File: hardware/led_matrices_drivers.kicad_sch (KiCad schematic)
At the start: 12 parts, among them U6 MAX7219, U7 MAX7219, U8 MAX7219, U9 MAX7219

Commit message: Removed comments on UART, added some footprints and started fixing rule checks
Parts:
- C12, C13, C14, C15: Manuf. Part # (none) -> GRM21BR71H104KA01L; Part Num GRM21BR71H104KA01L -> (none); Price/unit $0.0097 -> (none); Supplier Name (none) -> JLCPCB; Supplier Unit Price (none) -> $0.0097
- R10, R11, R12, R9: Manuf. Part # (none) -> CR0805F89531G; Part Num CR0805F89531G -> (none); Price/unit $0.0022 -> (none); Supplier Unit Price (none) -> $0.0022
- U6, U7, U8, U9: Manuf. Part # (none) -> MAX7219CWG+T; Part Num MAX7219CWG+T -> (none); Price/unit $2.6325 -> (none); Supplier Name (none) -> JLCPCB; Supplier Unit Price (none) -> $2.6325
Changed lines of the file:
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@@
 			)
 		)
-		(property "Part Num" "MAX7219CWG+T"
+		(property "Supplier Link" "https://jlcpcb.com/partdetail/10499-MAX7219CWGT/C9964"
 			(at 107.95 93.98 0)
 			(effects
@@
 			)
 		)
-		(property "Price/unit" "$2.6325"
+		(property "Supplier Name" "JLCPCB"
 			(at 107.95 93.98 0)
 			(effects
@@
 			)
 		)
-		(property "Supplier Link" "https://jlcpcb.com/partdetail/10499-MAX7219CWGT/C9964"
+		(property "Manuf. Part #" "MAX7219CWG+T"
+			(at 107.95 93.98 0)
+			(effects
+				(font
+					(size 1.27 1.27)
+				)
+				(hide yes)
+			)
+		)
+		(property "Supplier Unit Price" "$2.6325"
 			(at 107.95 93.98 0)
 			(effects
@@
 			)
 		)
-		(property "Part Num" "CR0805F89531G"
+		(property "Supplier Link" ""
 			(at 154.94 67.31 0)
 			(effects
@@
 			)
 		)
-		(property "Price/unit" " $0.0022"
+		(property "Supplier Name" ""
 			(at 154.94 67.31 0)
 			(effects
@@
 			)
 		)
-		(property "Supplier Link" ""
+		(property "Manuf. Part #" "CR0805F89531G"
+			(at 154.94 67.31 0)
+			(effects
+				(font
+					(size 1.27 1.27)
+				)
+				(hide yes)
+			)
+		)
+		(property "Supplier Unit Price" " $0.0022"
 			(at 154.94 67.31 0)
 			(effects
@@
 			)
 		)
-		(property "Part Num" "CR0805F89531G"
+		(property "Supplier Link" ""
 			(at 95.25 67.31 0)
 			(effects
@@
 			)
 		)
-		(property "Price/unit" " $0.0022"
+		(property "Supplier Name" ""
 			(at 95.25 67.31 0)
 			(effects
@@
 			)
 		)
-		(property "Supplier Link" ""
+		(property "Manuf. Part #" "CR0805F89531G"
+			(at 95.25 67.31 0)
+			(effects
+				(font
+					(size 1.27 1.27)
+				)
+				(hide yes)
+			)
+		)
+		(property "Supplier Unit Price" " $0.0022"
 			(at 95.25 67.31 0)
 			(effects
@@
 			)
 		)
-		(property "Part Num" "MAX7219CWG+T"
+		(property "Supplier Link" "https://jlcpcb.com/partdetail/10499-MAX7219CWGT/C9964"
 			(at 229.87 93.98 0)
 			(effects
@@
 			)
 		)
-		(property "Price/unit" "$2.6325"
+		(property "Supplier Name" "JLCPCB"
 			(at 229.87 93.98 0)
 			(effects
@@
 			)
 		)
-		(property "Supplier Link" "https://jlcpcb.com/partdetail/10499-MAX7219CWGT/C9964"
+		(property "Manuf. Part #" "MAX7219CWG+T"
+			(at 229.87 93.98 0)
+			(effects
+				(font
+					(size 1.27 1.27)
+				)
+				(hide yes)
+			)
+		)
+		(property "Supplier Unit Price" "$2.6325"
 			(at 229.87 93.98 0)
 			(effects
@@
 			)
 		)
-		(property "Price/unit" " $0.0022"
+		(property "Package" "0805"
 			(at 34.29 67.31 0)
 			(effects
@@
 			)
 		)
-		(property "Part Num" "CR0805F89531G"
+		(property "Supplier Name" ""
 			(at 34.29 67.31 0)
 			(effects
@@
 			)
 		)
-		(property "Package" "0805"
+		(property "Manuf. Part #" "CR0805F89531G"
+			(at 34.29 67.31 0)
+			(effects
+				(font
+					(size 1.27 1.27)
+				)
+				(hide yes)
+			)
+		)
+		(property "Supplier Unit Price" " $0.0022"
 			(at 34.29 67.31 0)
 			(effects
@@
 			)
 		)
-		(property "Price/unit" "$2.6325"
+		(property "Package" "SOIC-24-300mil"
 			(at 46.99 93.98 0)
 			(effects
@@
 			)
 		)
-		(property "Part Num" "MAX7219CWG+T"
+		(property "Supplier Name" "JLCPCB"
 			(at 46.99 93.98 0)
 			(effects
@@
 			)
 		)
-		(property "Package" "SOIC-24-300mil"
+		(property "Manuf. Part #" "MAX7219CWG+T"
+			(at 46.99 93.98 0)
+			(effects
+				(font
+					(size 1.27 1.27)
+				)
+				(hide yes)
+			)
+		)
+		(property "Supplier Unit Price" "$2.6325"
 			(at 46.99 93.98 0)
 			(effects
@@
 			)
 		)
-		(property "Part Num" "GRM21BR71H104KA01L"
+		(property "Supplier Link" "https://jlcpcb.com/partdetail/MurataElectronics-GRM21BR71H104KA01L/C77082"
 			(at 232.41 64.77 0)
 			(effects
@@
 			)
 		)
-		(property "Price/unit" "$0.0097"
+		(property "Supplier Name" "JLCPCB"
 			(at 232.41 64.77 0)
 			(effects
@@
 			)
 		)
-		(property "Supplier Link" "https://jlcpcb.com/partdetail/MurataElectronics-GRM21BR71H104KA01L/C77082"
+		(property "Manuf. Part #" "GRM21BR71H104KA01L"
+			(at 232.41 64.77 0)
+			(effects
+				(font
+					(size 1.27 1.27)
+				)
+				(hide yes)
+			)
+		)
+		(property "Supplier Unit Price" "$0.0097"
 			(at 232.41 64.77 0)
 			(effects
@@
 			)
 		)
-		(property "Part Num" "MAX7219CWG+T"
+		(property "Supplier Link" "https://jlcpcb.com/partdetail/10499-MAX7219CWGT/C9964"
 			(at 167.64 93.98 0)
 			(effects
@@
 			)
 		)
-		(property "Price/unit" "$2.6325"
+		(property "Supplier Name" "JLCPCB"
 			(at 167.64 93.98 0)
 			(effects
@@
 			)
 		)
-		(property "Supplier Link" "https://jlcpcb.com/partdetail/10499-MAX7219CWGT/C9964"
+		(property "Manuf. Part #" "MAX7219CWG+T"
+			(at 167.64 93.98 0)
+			(effects
+				(font
+					(size 1.27 1.27)
+				)
+				(hide yes)
+			)
+		)
+		(property "Supplier Unit Price" "$2.6325"
 			(at 167.64 93.98 0)
 			(effects
@@
 			)
 		)
-		(property "Part Num" "GRM21BR71H104KA01L"
+		(property "Supplier Link" "https://jlcpcb.com/partdetail/MurataElectronics-GRM21BR71H104KA01L/C77082"
 			(at 170.18 64.77 0)
 			(effects
@@
 			)
 		)
-		(property "Price/unit" "$0.0097"
+		(property "Supplier Name" "JLCPCB"
 			(at 170.18 64.77 0)
 			(effects
@@
 			)
 		)
-		(property "Supplier Link" "https://jlcpcb.com/partdetail/MurataElectronics-GRM21BR71H104KA01L/C77082"
+		(property "Manuf. Part #" "GRM21BR71H104KA01L"
+			(at 170.18 64.77 0)
+			(effects
+				(font
+					(size 1.27 1.27)
+				)
+				(hide yes)
+			)
+		)
+		(property "Supplier Unit Price" "$0.0097"
 			(at 170.18 64.77 0)
 			(effects
@@
 			)
 		)
-		(property "Part Num" "GRM21BR71H104KA01L"
+		(property "Supplier Link" "https://jlcpcb.com/partdetail/MurataElectronics-GRM21BR71H104KA01L/C77082"
 			(at 110.49 64.77 0)
 			(effects
@@
 			)
 		)
-		(property "Price/unit" "$0.0097"
+		(property "Supplier Name" "JLCPCB"
 			(at 110.49 64.77 0)
 			(effects
@@
 			)
 		)
-		(property "Supplier Link" "https://jlcpcb.com/partdetail/MurataElectronics-GRM21BR71H104KA01L/C77082"
+		(property "Manuf. Part #" "GRM21BR71H104KA01L"
+			(at 110.49 64.77 0)
+			(effects
+				(font
+					(size 1.27 1.27)
+				)
+				(hide yes)
+			)
+		)
+		(property "Supplier Unit Price" "$0.0097"
 			(at 110.49 64.77 0)
 			(effects
@@
 			)
 		)
-		(property "Part Num" "GRM21BR71H104KA01L"
+		(property "Supplier Link" "https://jlcpcb.com/partdetail/MurataElectronics-GRM21BR71H104KA01L/C77082"
 			(at 49.53 64.77 0)
 			(effects
@@
 			)
 		)
-		(property "Price/unit" "$0.0097"
+		(property "Supplier Name" "JLCPCB"
 			(at 49.53 64.77 0)
 			(effects
@@
 			)
 		)
-		(property "Supplier Link" "https://jlcpcb.com/partdetail/MurataElectronics-GRM21BR71H104KA01L/C77082"
+		(property "Manuf. Part #" "GRM21BR71H104KA01L"
+			(at 49.53 64.77 0)
+			(effects
+				(font
+					(size 1.27 1.27)
+				)
+				(hide yes)
+			)
+		)
+		(property "Supplier Unit Price" "$0.0097"
 			(at 49.53 64.77 0)
 			(effects
@@
 			)
 		)
-		(property "Part Num" "CR0805F89531G"
-			(at 217.17 67.31 0)
-			(effects
-				(font
-					(size 1.27 1.27)
-				)
-				(hide yes)
-			)
-		)
-		(property "Price/unit" " $0.0022"
-			(at 217.17 67.31 0)
-			(effects
-				(font
-					(size 1.27 1.27)
-				)
-				(hide yes)
-			)
-		)
 		(property "Supplier Link" ""
 			(at 217.17 67.31 0)
 			(effects
+				(font
+					(size 1.27 1.27)
+				)
+				(hide yes)
+			)
+		)
+		(property "Supplier Name" ""
+			(at 217.17 67.31 0)
+			(effects
+				(font
+					(size 1.27 1.27)
+				)
+				(hide yes)
+			)
+		)
+		(property "Manuf. Part #" "CR0805F89531G"
+			(at 217.17 67.31 0)
+			(effects
+				(font
+					(size 1.27 1.27)
+				)
+				(hide yes)
+			)
+		)
+		(property "Supplier Unit Price" " $0.0022"
+			(at 217.17 67.31 0)
+			(effects

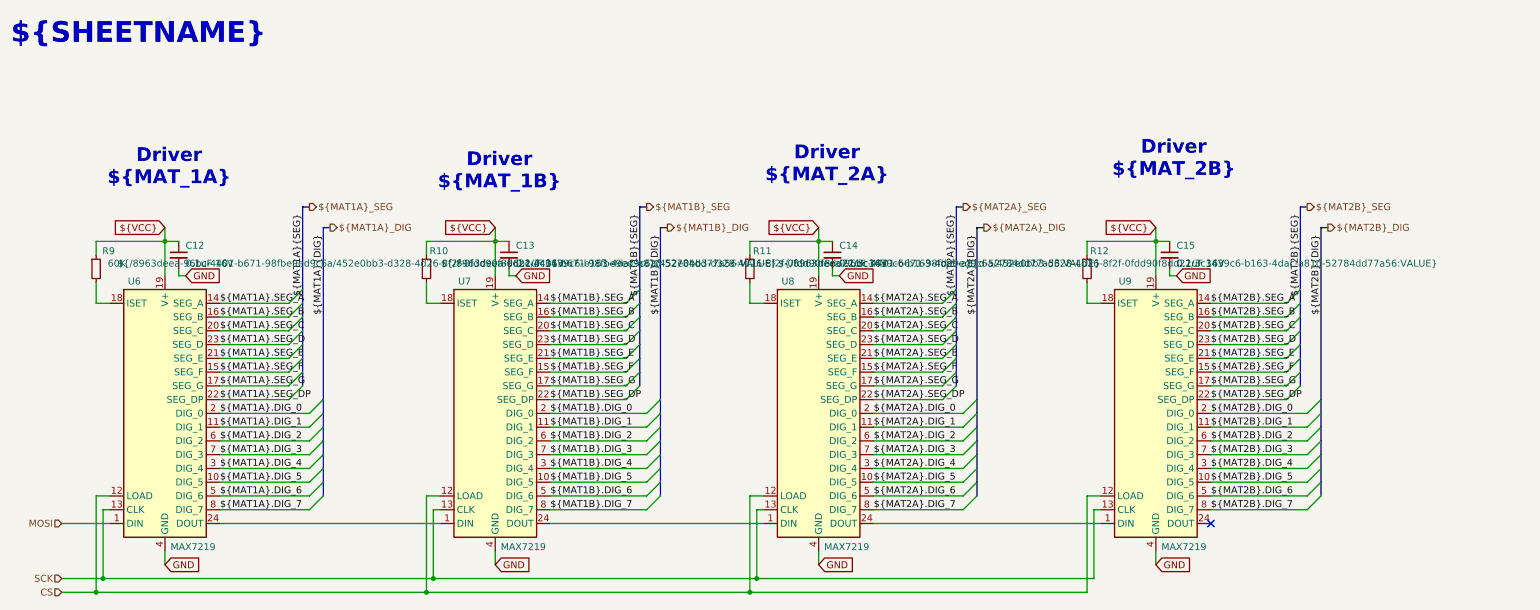
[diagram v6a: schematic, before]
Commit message: Added many footprints and populated part of the property tables
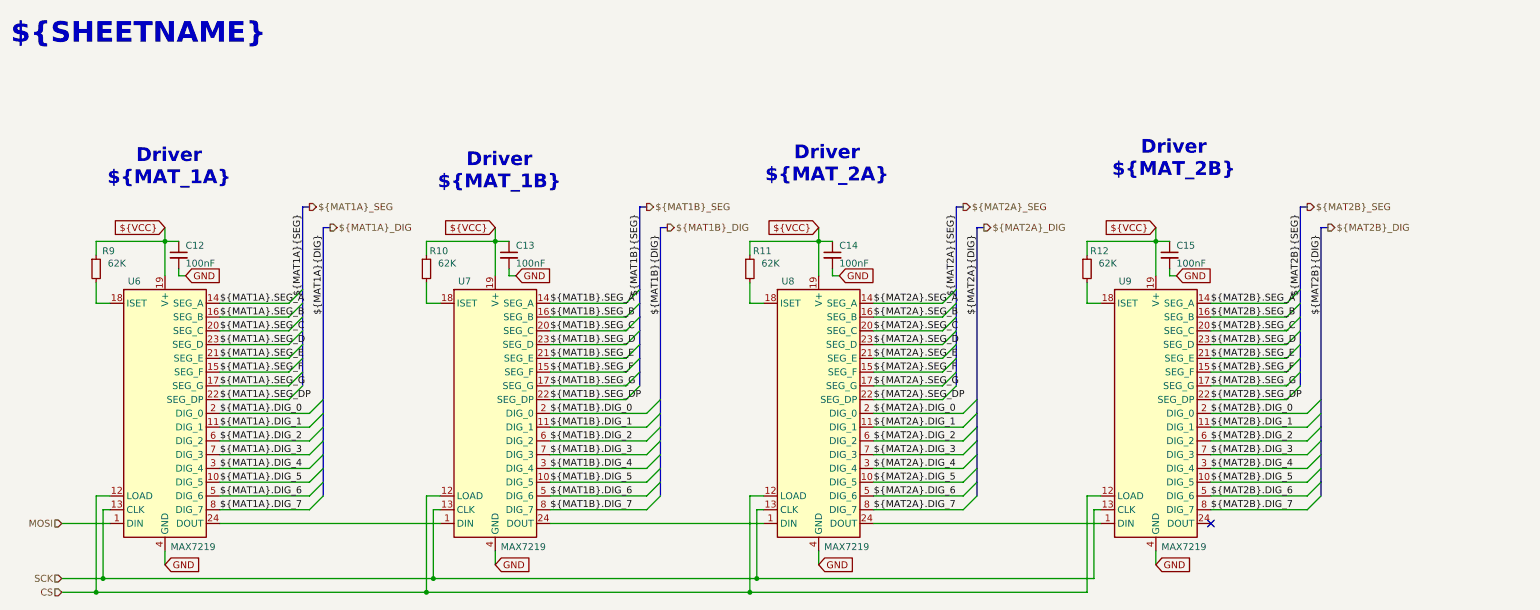
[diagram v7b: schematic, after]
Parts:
- C12, C13, C14, C15: value 0.1uF 16V -> 100nF; footprint (none) -> Capacitor_SMD:C_0805_2012Metric_Pad1.18x1.45mm_HandSolder; Manuf. Name (none) -> Murata Electronics; Supplier Link https://jlcpcb.com/partdetail/MurataElectronics-GRM21BR71H104KA01L/C77082 -> https://jlcpcb.com/partdetail/MurataElectronics-GRM21BR71H104KA01L/C77082; Supplier Part # (none) -> C77082; Supplier Unit Price $0.0097 -> $0.0099
- R10, R11, R12: value ${/8963deea-96bc-4401-b671-98fbe9ed9c6a/452e0bb3-d328-4d26-8f2f-0fdd90f8dd22/3c3439c6-b163-4dac-a81d-52784dd77a56:VALUE} -> 62K; footprint (none) -> Resistor_SMD:R_0805_2012Metric_Pad1.20x1.40mm_HandSolder; Manuf. Name (none) -> UNI-ROYAL(Uniroyal Elec); Manuf. Part # CR0805F89531G -> 0805W8F6202T5E; Supplier Link (none) -> https://jlcpcb.com/partdetail/18471-0805W8F6202T5E/C17783; Supplier Name (none) -> JLCPCB; Supplier Part # (none) -> C17783; Supplier Unit Price $0.0022 -> $0.0019
- R9: value 60K -> 62K; footprint (none) -> Resistor_SMD:R_0805_2012Metric_Pad1.20x1.40mm_HandSolder; Manuf. Name (none) -> UNI-ROYAL(Uniroyal Elec); Manuf. Part # CR0805F89531G -> 0805W8F6202T5E; Supplier Link (none) -> https://jlcpcb.com/partdetail/18471-0805W8F6202T5E/C17783; Supplier Name (none) -> JLCPCB; Supplier Part # (none) -> C17783; Supplier Unit Price $0.0022 -> $0.0019

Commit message: Completed the property teble except for the cyristal oscilator
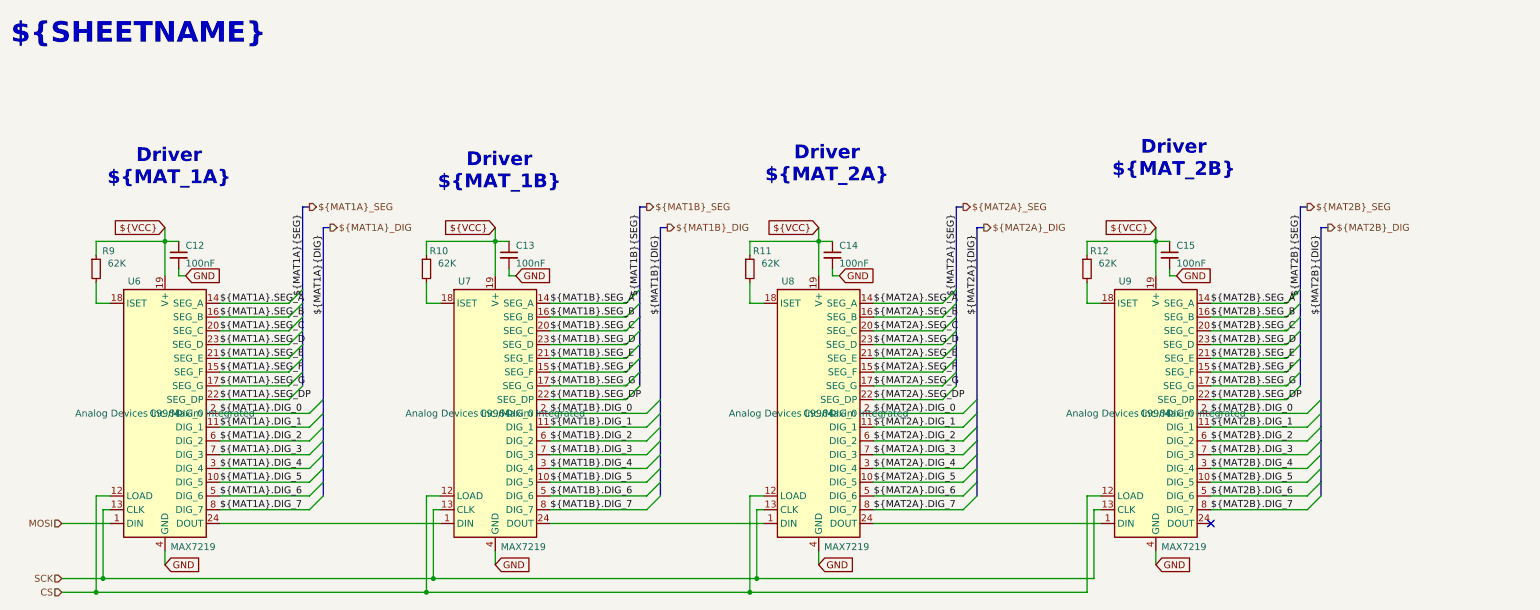
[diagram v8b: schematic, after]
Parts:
- U6, U7, U8, U9: footprint (none) -> Package_SO:SOIC-24W_7.5x15.4mm_P1.27mm; Manuf. Name (none) -> Analog Devices Inc./Maxim Integrated; Supplier Part # (none) -> C9964; Supplier Unit Price $2.6325 -> $3.0975
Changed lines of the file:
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@@
 			)
 		)
-		(property "Footprint" ""
+		(property "Footprint" "Package_SO:SOIC-24W_7.5x15.4mm_P1.27mm"
 			(at 106.68 92.71 0)
 			(effects
@@
 			)
 		)
-		(property "Supplier Unit Price" "$2.6325"
+		(property "Supplier Unit Price" " $3.0975"
 			(at 107.95 93.98 0)
 			(effects
@@
 				)
 				(hide yes)
+			)
+		)
+		(property "Manuf. Name" "Analog Devices Inc./Maxim Integrated"
+			(at 107.95 93.98 0)
+			(effects
+				(font
+					(size 1.27 1.27)
+				)
+			)
+		)
+		(property "Supplier Part #" "C9964"
+			(at 107.95 93.98 0)
+			(effects
+				(font
+					(size 1.27 1.27)
+				)
 			)
 		)
@@
 			)
 		)
-		(property "Description" "Resistor, small symbol"
+		(property "Description" "62k, 0805"
 			(at 154.94 67.31 0)
 			(effects
@@
 			)
 		)
-		(property "Description" "Resistor, small symbol"
+		(property "Description" "62k, 0805"
 			(at 95.25 67.31 0)
 			(effects
@@
 			)
 		)
-		(property "Footprint" ""
+		(property "Footprint" "Package_SO:SOIC-24W_7.5x15.4mm_P1.27mm"
 			(at 228.6 92.71 0)
 			(effects
@@
 			)
 		)
-		(property "Supplier Unit Price" "$2.6325"
+		(property "Supplier Unit Price" " $3.0975"
 			(at 229.87 93.98 0)
 			(effects
@@
 				)
 				(hide yes)
+			)
+		)
+		(property "Manuf. Name" "Analog Devices Inc./Maxim Integrated"
+			(at 229.87 93.98 0)
+			(effects
+				(font
+					(size 1.27 1.27)
+				)
+			)
+		)
+		(property "Supplier Part #" "C9964"
+			(at 229.87 93.98 0)
+			(effects
+				(font
+					(size 1.27 1.27)
+				)
 			)
 		)
@@
 			)
 		)
-		(property "Description" "Resistor, small symbol"
+		(property "Description" "62k, 0805"
 			(at 34.29 67.31 0)
 			(effects
@@
 			)
 		)
-		(property "Footprint" ""
+		(property "Footprint" "Package_SO:SOIC-24W_7.5x15.4mm_P1.27mm"
 			(at 45.72 92.71 0)
 			(effects
@@
 			)
 		)
-		(property "Supplier Unit Price" "$2.6325"
+		(property "Supplier Unit Price" " $3.0975"
 			(at 46.99 93.98 0)
 			(effects
@@
 				)
 				(hide yes)
+			)
+		)
+		(property "Manuf. Name" "Analog Devices Inc./Maxim Integrated"
+			(at 46.99 93.98 0)
+			(effects
+				(font
+					(size 1.27 1.27)
+				)
+			)
+		)
+		(property "Supplier Part #" "C9964"
+			(at 46.99 93.98 0)
+			(effects
+				(font
+					(size 1.27 1.27)
+				)
 			)
 		)
@@
 			)
 		)
-		(property "Footprint" ""
+		(property "Footprint" "Package_SO:SOIC-24W_7.5x15.4mm_P1.27mm"
 			(at 166.37 92.71 0)
 			(effects
@@
 			)
 		)
-		(property "Supplier Unit Price" "$2.6325"
+		(property "Supplier Unit Price" " $3.0975"
 			(at 167.64 93.98 0)
 			(effects
@@
 				)
 				(hide yes)
+			)
+		)
+		(property "Manuf. Name" "Analog Devices Inc./Maxim Integrated"
+			(at 167.64 93.98 0)
+			(effects
+				(font
+					(size 1.27 1.27)
+				)
+			)
+		)
+		(property "Supplier Part #" "C9964"
+			(at 167.64 93.98 0)
+			(effects
+				(font
+					(size 1.27 1.27)
+				)
 			)
 		)
@@
 			)
 		)
-		(property "Description" "Resistor, small symbol"
+		(property "Description" "62k, 0805"
 			(at 217.17 67.31 0)
 			(effects
